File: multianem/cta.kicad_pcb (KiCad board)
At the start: 2 copper layers, 198.1 x 99.1 mm, 150 parts, among them Q1 TIP120, Q2 TIP120, Q3 TIP120, Q4 TIP120, Q5 TIP120, Q6 TIP120, Q7 TIP120, Q8 TIP120, U1 OP07, U2 OP07, U3 OP07, U4 OP07, U5 OP07, U6 OP07, U7 OP07, U8 OP07

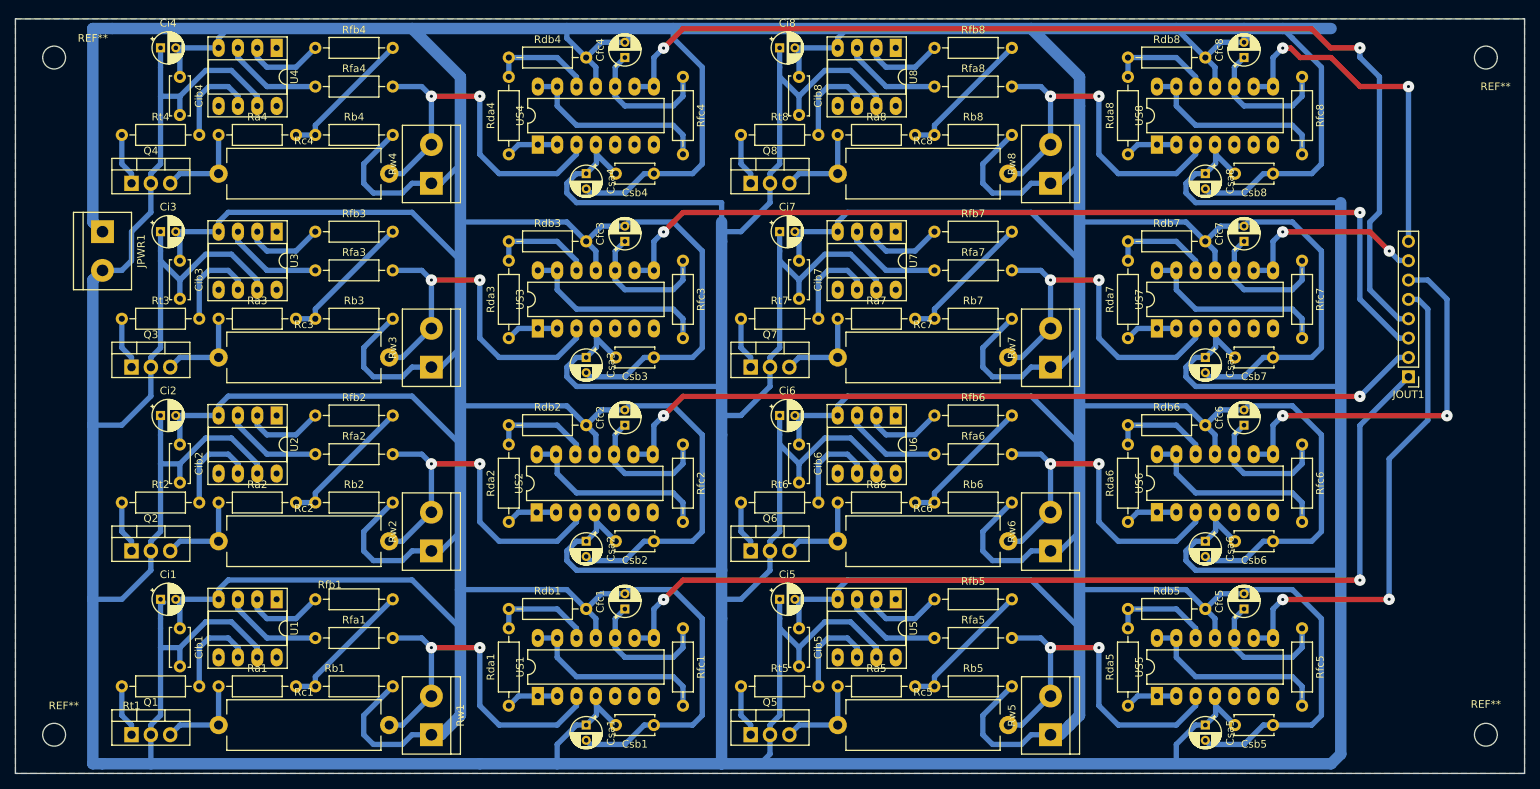
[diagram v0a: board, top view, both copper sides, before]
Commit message: Added more power inputs to the board
To make it easy to stack the 8 channel boards, added a Vcc and GND inputs.
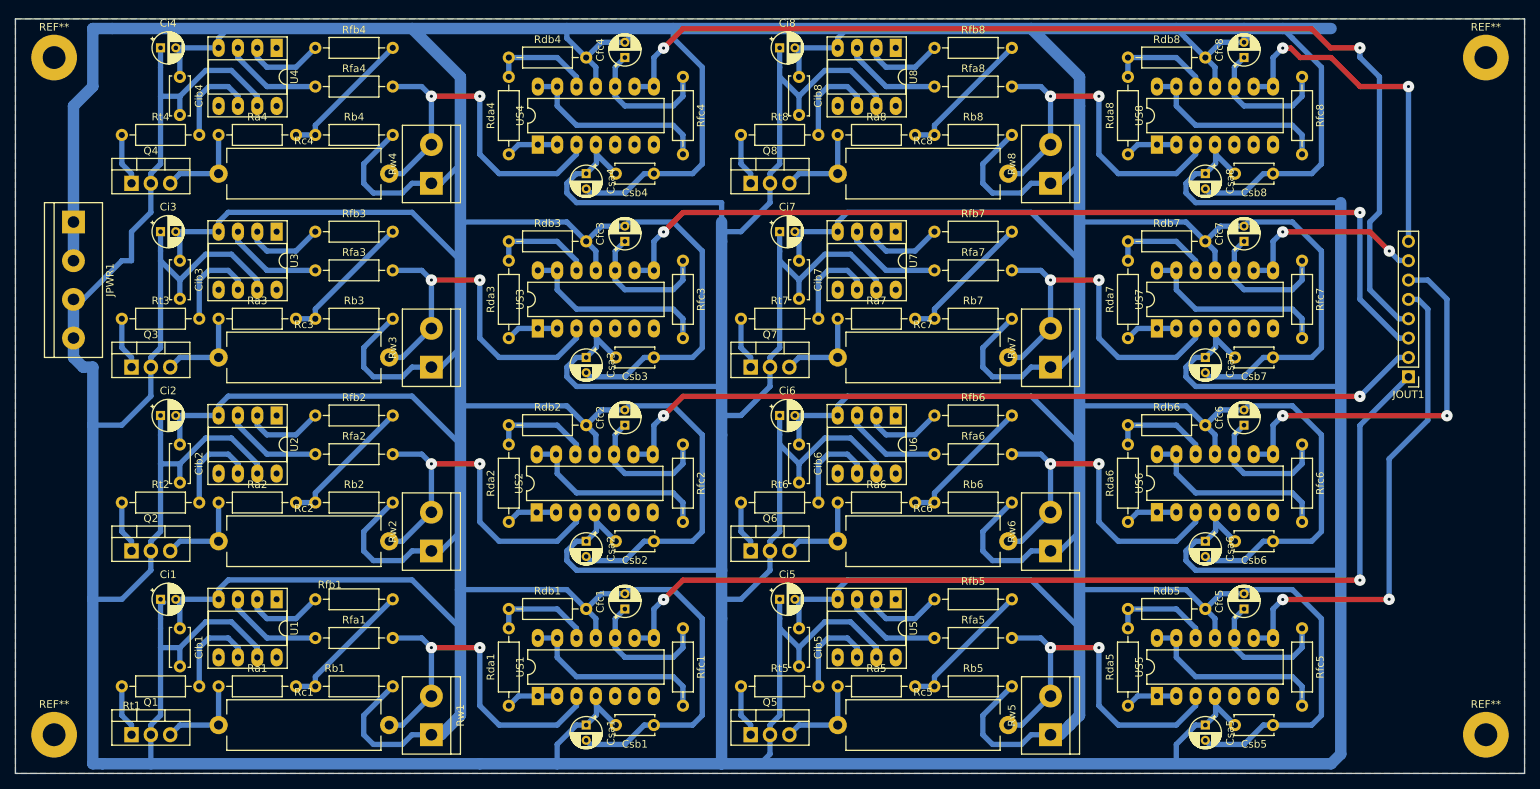
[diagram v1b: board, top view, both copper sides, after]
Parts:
- removed the REF** at (43.2, 31.8)
- removed the REF** at (43.2, 120.7)
- removed the REF** at (231.1, 120.7)
- removed the REF** at (231.1, 31.8)
- added REF**: MountingHole_3mm_Pad, MountingHole:MountingHole_3mm_Pad, F.Cu at (231.1, 31.8)
- added REF**: MountingHole_3mm_Pad, MountingHole:MountingHole_3mm_Pad, F.Cu at (231.1, 120.7)
- added REF**: MountingHole_3mm_Pad, MountingHole:MountingHole_3mm_Pad, F.Cu at (43.2, 120.7)
- added REF**: MountingHole_3mm_Pad, MountingHole:MountingHole_3mm_Pad, F.Cu at (43.2, 31.8)
- JPWR1: value Conn_01x02 -> Conn_01x04; footprint TerminalBlock:TerminalBlock_bornier-2_P5.08mm -> TerminalBlock:TerminalBlock_bornier-4_P5.08mm
- moved JPWR1 4.02 mm to (45.7, 53.3)
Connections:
- JPWR1 pad 2: VCC -> GND
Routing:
- net GND: track 1521.8 -> 1526.1 mm
- net VCC: track 991.6 -> 994.5 mm
